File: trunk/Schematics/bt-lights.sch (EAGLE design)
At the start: 25 parts, among them IC1 MAX6966

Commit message: ADDED:  - the world famous icon  - new protocol revision  - schematics and layout (prelim)
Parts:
- added R11: 10k, resistor:R-EU_0207/7
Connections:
- net AT: now also R11.2
- net GND: now also R11.1
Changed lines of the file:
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@@
 <setting verticaltext="up"/>
 </settings>
-<grid distance="0.1" unitdist="inch" unit="inch" style="lines" multiple="1" display="yes" altdistance="0.01" altunitdist="inch" altunit="inch"/>
+<grid distance="0.1" unitdist="inch" unit="inch" style="lines" multiple="1" display="no" altdistance="0.01" altunitdist="inch" altunit="inch"/>
 <layers>
 <layer number="1" name="Top" color="4" fill="1" visible="no" active="no"/>
@@
 <part name="+3V3" library="supply1" deviceset="+3V3" device=""/>
 <part name="GND3" library="supply1" deviceset="GND" device=""/>
+<part name="R11" library="resistor" deviceset="R-EU_" device="0207/7" value="10k"/>
 </parts>
 <sheets>
@@
 <instance part="+3V3" gate="G$1" x="68.58" y="101.6"/>
 <instance part="GND3" gate="1" x="119.38" y="30.48"/>
+<instance part="R11" gate="G$1" x="127" y="43.18" rot="R90"/>
 </instances>
 <busses>
@@
 <junction x="119.38" y="38.1"/>
 <junction x="119.38" y="35.56"/>
+<pinref part="R11" gate="G$1" pin="1"/>
+<wire x1="127" y1="38.1" x2="127" y2="35.56" width="0.1524" layer="91"/>
+<wire x1="127" y1="35.56" x2="119.38" y2="35.56" width="0.1524" layer="91"/>
 </segment>
 </net>
@@
 <segment>
 <pinref part="BT_INTERFACE" gate="G$1" pin="PIO11"/>
-<wire x1="114.3" y1="53.34" x2="119.38" y2="53.34" width="0.1524" layer="91"/>
-<label x="119.38" y="53.34" size="1.016" layer="95" font="vector" xref="yes"/>
-</segment>
-</net>
+<wire x1="114.3" y1="53.34" x2="127" y2="53.34" width="0.1524" layer="91"/>
+<label x="129.54" y="53.34" size="1.016" layer="95" font="vector" xref="yes"/>
+<pinref part="R11" gate="G$1" pin="2"/>
+<wire x1="127" y1="53.34" x2="129.54" y2="53.34" width="0.1524" layer="91"/>
+<wire x1="127" y1="53.34" x2="127" y2="48.26" width="0.1524" layer="91"/>
+<junction x="127" y="53.34"/>
+</segment>
+</net>

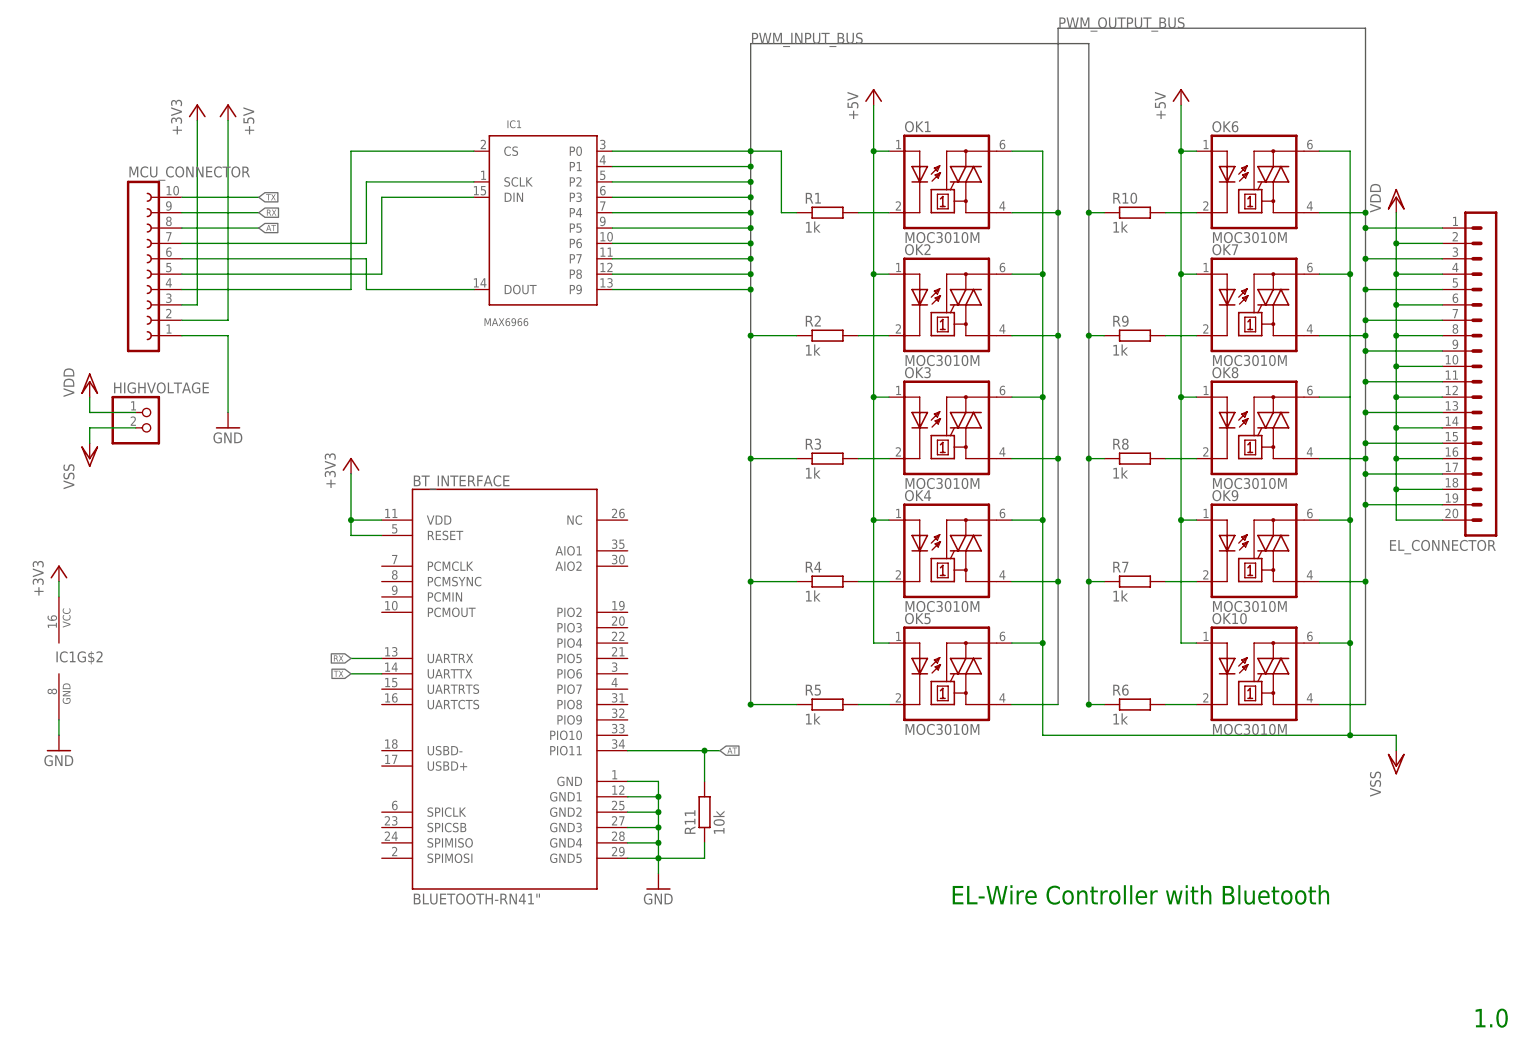
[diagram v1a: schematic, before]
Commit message: UPDATE:  - new hardware fix in schematic  - new commands in test gui  - new pinning documented ADDED:  - NETDUINO schematic
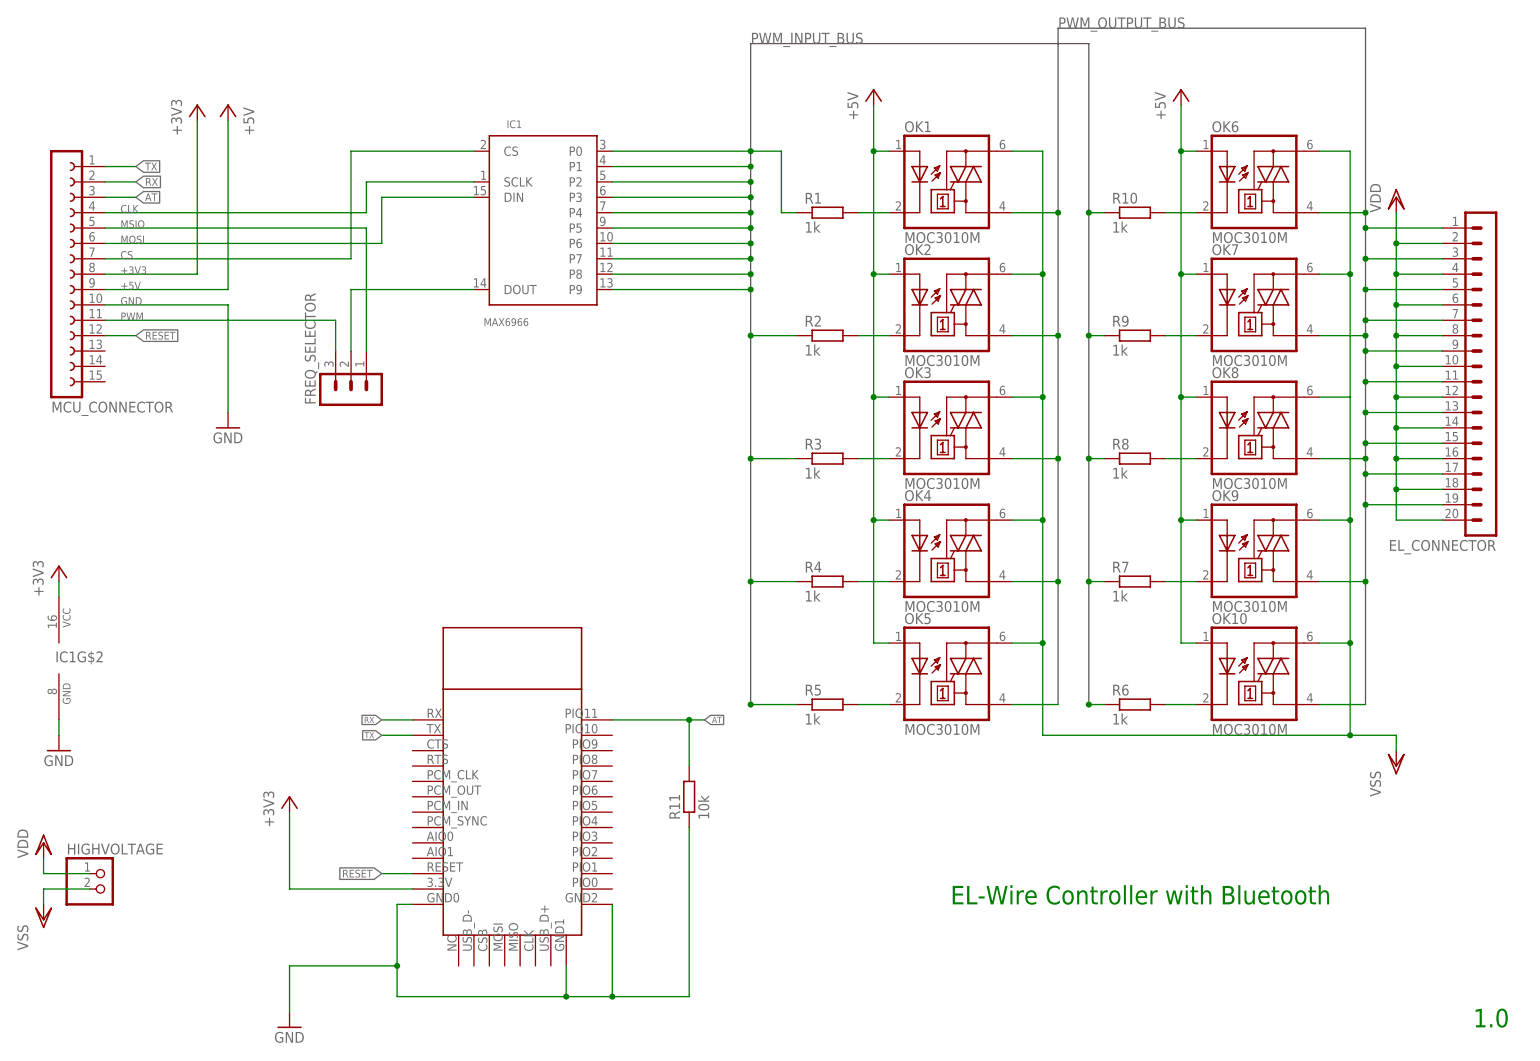
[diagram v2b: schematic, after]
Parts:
- removed BT_INTERFACE: BLUETOOTH-RN41", SparkFun-RF:BLUETOOTH-RN41"
- added FREQ_SELECTOR: (no value), con-lstb:MA03-1
- added HC0305: HC0305, HC0305:HC0305
- MCU_CONNECTOR: device con-lsta:FE10-1 -> con-lsta:FE15-1
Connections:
- removed net N$1: IC1G$1.CS, MCU_CONNECTOR.4
- removed net N$2: IC1G$1.SCLK, MCU_CONNECTOR.7
- removed net N$3: IC1G$1.DIN, MCU_CONNECTOR.5
- removed net N$4: IC1G$1.DOUT, MCU_CONNECTOR.6
- new net CLK: IC1G$1.SCLK, MCU_CONNECTOR.4
- new net CS: IC1G$1.CS, MCU_CONNECTOR.7
- new net MOSI: IC1G$1.DIN, MCU_CONNECTOR.6
- new net MSIO: FREQ_SELECTOR.1, MCU_CONNECTOR.5
- new net N$16: FREQ_SELECTOR.2, IC1G$1.DOUT
- new net PWM: FREQ_SELECTOR.3, MCU_CONNECTOR.11
- new net RESET: MCU_CONNECTOR.12
- net +3V3: now also MCU_CONNECTOR.8; no longer BT_INTERFACE.RESET, BT_INTERFACE.VDD, MCU_CONNECTOR.3
- net +5V: now also MCU_CONNECTOR.9; no longer MCU_CONNECTOR.2
- net AT: now also MCU_CONNECTOR.3; no longer BT_INTERFACE.PIO11, MCU_CONNECTOR.8
- net GND: now also MCU_CONNECTOR.10; no longer BT_INTERFACE.GND, BT_INTERFACE.GND1, BT_INTERFACE.GND2, BT_INTERFACE.GND3, BT_INTERFACE.GND4, BT_INTERFACE.GND5, MCU_CONNECTOR.1
- net RX: now also MCU_CONNECTOR.2; no longer BT_INTERFACE.UARTRX, MCU_CONNECTOR.9
- net TX: now also MCU_CONNECTOR.1; no longer BT_INTERFACE.UARTTX, MCU_CONNECTOR.10
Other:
- moved on the sheet: HIGHVOLTAGE, R11
